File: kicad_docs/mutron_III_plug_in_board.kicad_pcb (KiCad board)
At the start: 2 copper layers, 58.4 x 50.8 mm, 46 parts, among them J1 Conn_01x04_Male, J2 Conn_01x04_Male, J3 Conn_01x04_Male, J4 Conn_01x08_Male, J5 HP-BP-LP, Q1 BC857, Q2 BCM847, Q3 BC847, U1 TL072, U2 RC4558, U3 vactrol, U4 vactrol, U5 RC4558

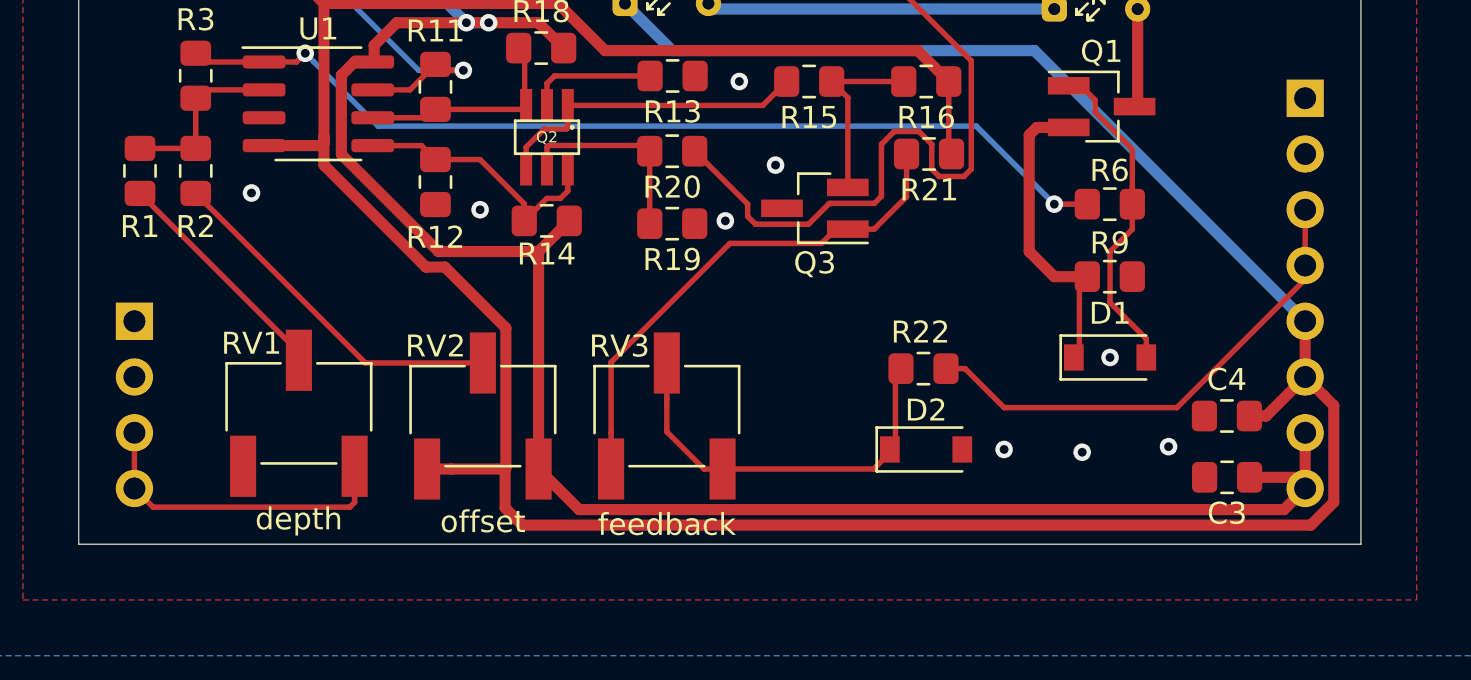
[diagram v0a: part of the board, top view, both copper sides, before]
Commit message: change trimmers to cheaper TH type
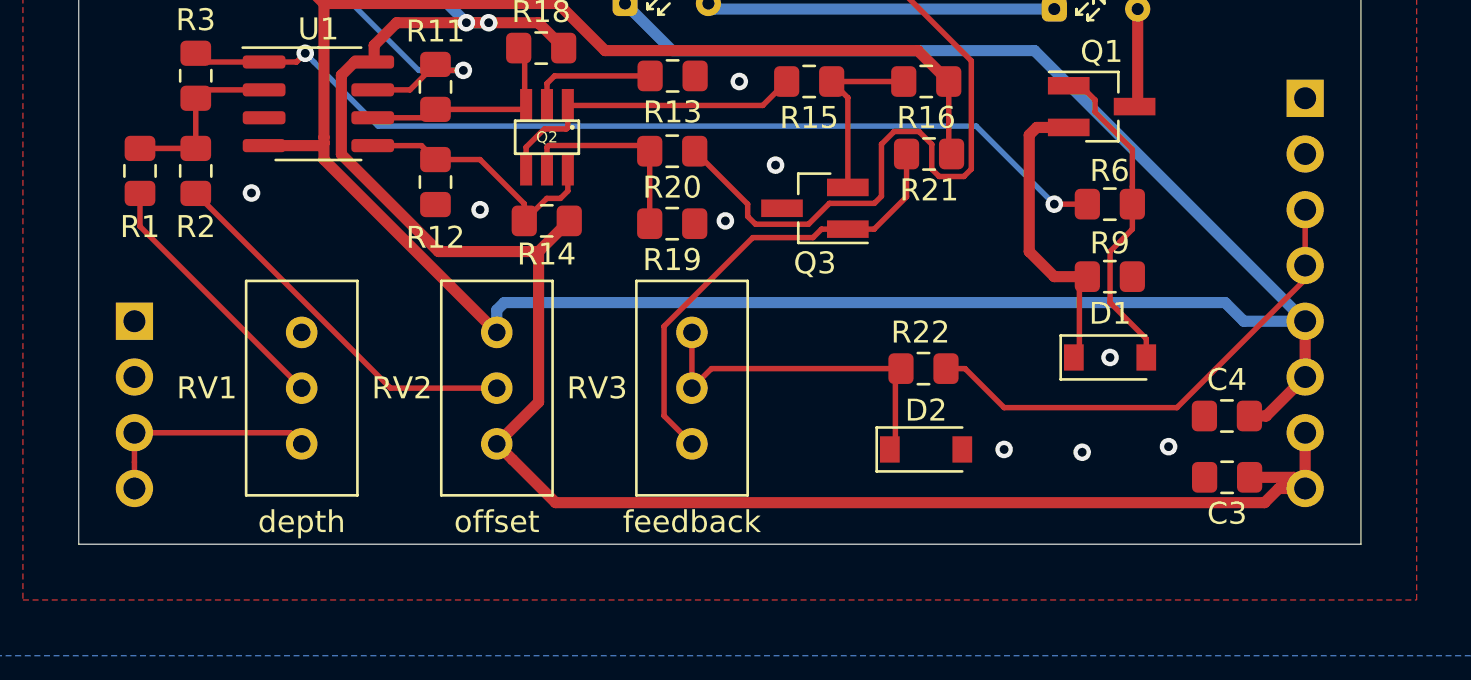
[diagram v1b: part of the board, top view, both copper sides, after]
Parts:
- RV1, RV2, RV3: footprint Potentiometer_SMD:Potentiometer_Bourns_3269W_Vertical -> Potentiometer_THT:Potentiometer_Bourns_3296W_Vertical
- moved RV3 3.98 mm to (129.5, 91.9), turned to 90 degrees
- moved RV2 3.86 mm to (120.7, 91.9), turned to 90 degrees
- moved RV1 3.69 mm to (111.8, 91.9), turned to 90 degrees
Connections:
- RV3 pad 1: Net-(Q3-Pad1) -> Net-(D2-Pad1)
- RV3 pad 3: Net-(D2-Pad1) -> Net-(Q3-Pad1)
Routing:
- net -12V: track 222.3 -> 203.4 mm
- net Net-(J1-Pad3): track 14.7 -> 10.4 mm
- net Net-(Q3-Pad1): track 23.4 -> 21.3 mm
- net Net-(D2-Pad1): track 18.3 -> 16.3 mm
- net +12V: track 136.7 -> 138.5 mm
- net Net-(R1-Pad2): track 10.6 -> 11.9 mm
- net Net-(R2-Pad2): track 16.3 -> 17.4 mm
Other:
- board text added: "github.com/JordanAceto/mutron_III_plug_in_board rev 1.0 2019-07-10"
